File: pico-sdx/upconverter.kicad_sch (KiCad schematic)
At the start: 52 parts, among them T2 Transformer_SP_1S, U4 LM321, U5 74HC74, U6 4066, U7 OPA1602

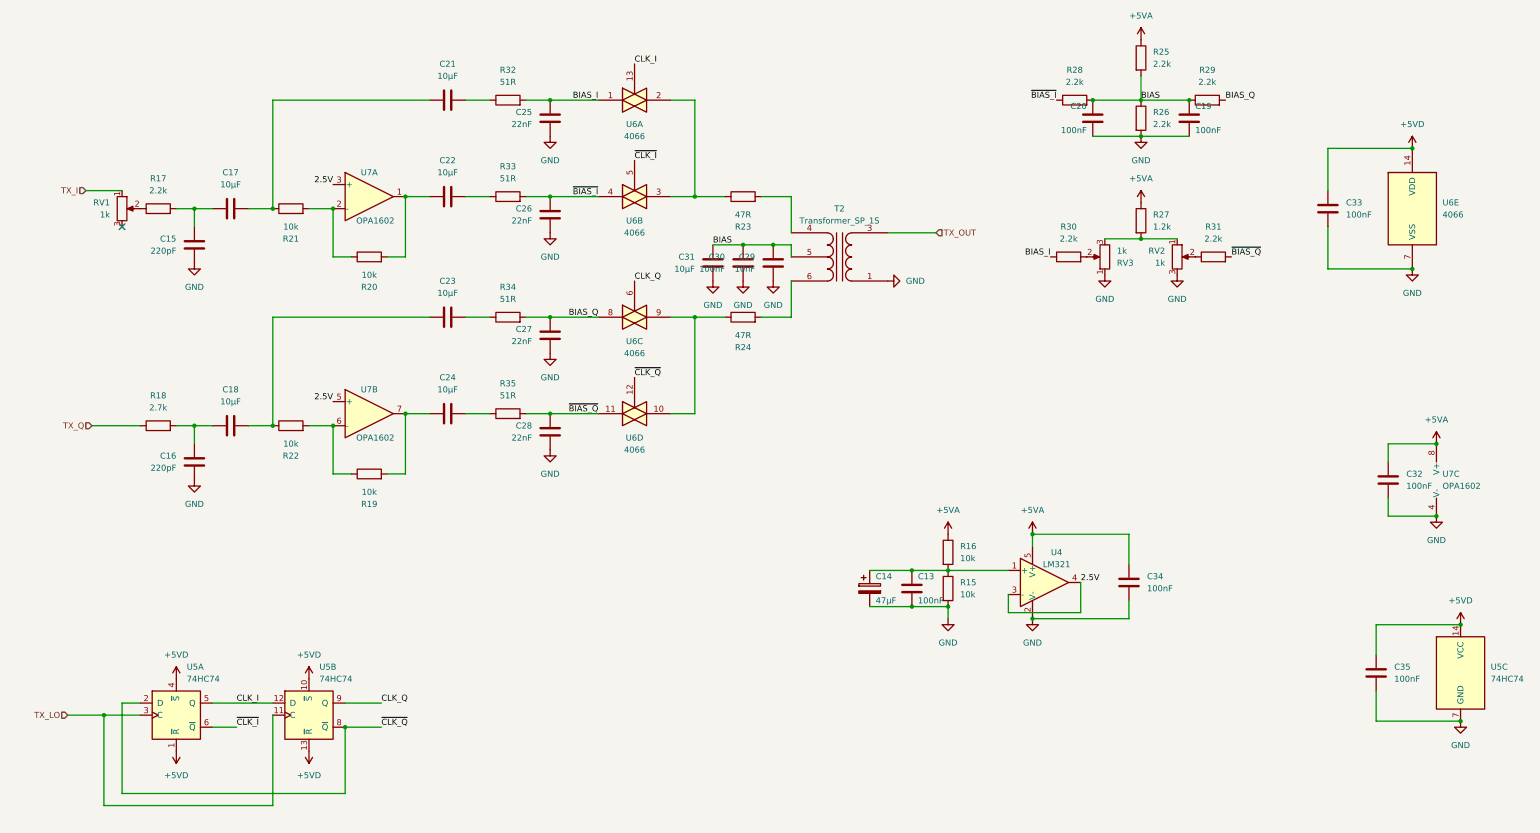
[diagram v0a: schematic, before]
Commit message: add documentation and RaspberryPi Pico
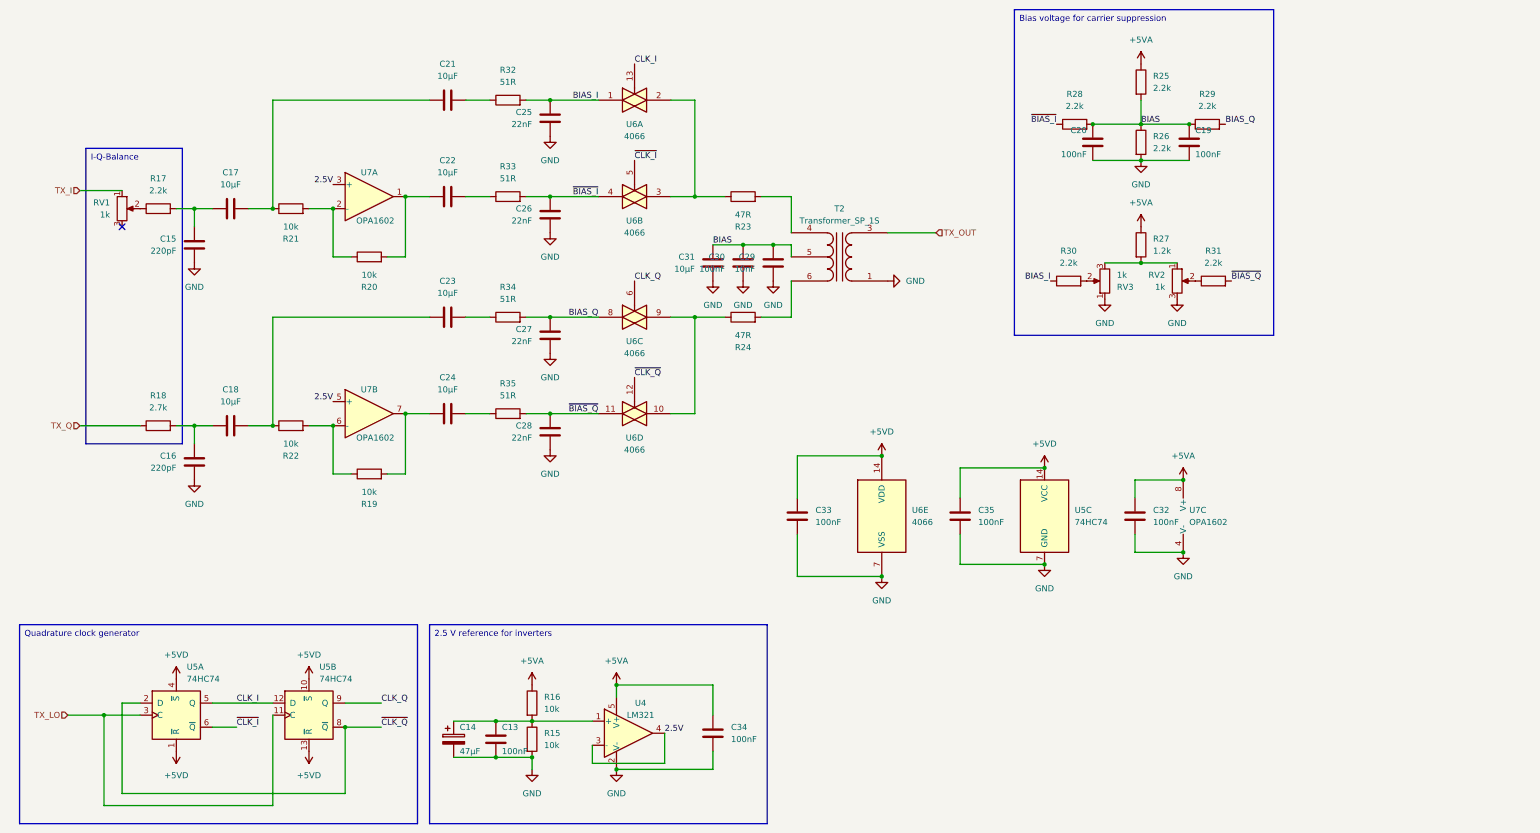
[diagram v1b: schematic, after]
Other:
- moved on the sheet: C13, C14, C19, C20, C32, C33, C34, C35, R15, R16, R25, R26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

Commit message: routed with filter relays without PA
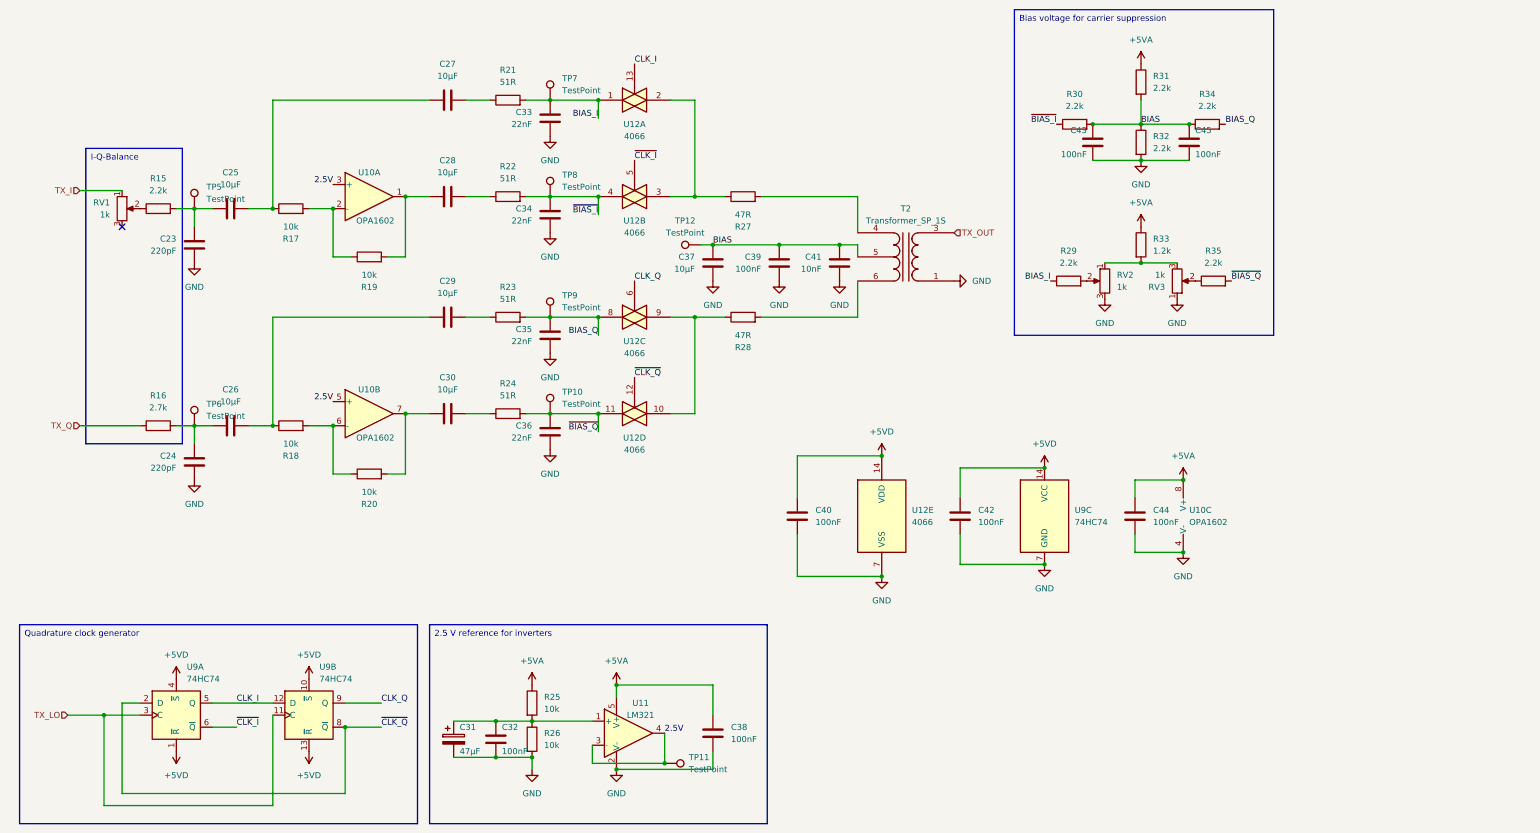
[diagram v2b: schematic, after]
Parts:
- added TP10, TP11, TP12, TP5, TP6, TP7, TP8, TP9: TestPoint, TestPoint:TestPoint_Loop_D1.80mm_Drill1.0mm_Beaded, symbol Connector:TestPoint
- renumbered C15 to C23, C16 to C24, C17 to C25, C18 to C26, C21 to C27, C22 to C28, C23 to C29, C24 to C30, C14 to C31, C13 to C32, C25 to C33, C26 to C34, C27 to C35, C28 to C36, C31 to C37, C34 to C38, C30 to C39, C33 to C40, C29 to C41, C35 to C42, C20 to C43, C32 to C44, C19 to C45, R17 to R15, R18 to R16, R21 to R17, R22 to R18, R20 to R19, R19 to R20, R32 to R21, R33 to R22, R34 to R23, R35 to R24, R16 to R25, R15 to R26, R23 to R27, R24 to R28, R30 to R29, R28 to R30, R25 to R31, R26 to R32, R27 to R33, R29 to R34, R31 to R35, RV3 to RV2, RV2 to RV3, U7 to U10, U4 to U11, U6 to U12, U5 to U9
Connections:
- net 2.5V: now also TP11.1
- net BIAS: now also TP12.1
- net BIAS_I: now also TP7.1
- net BIAS_Q: now also TP9.1
- net GND: now also RV2.3, RV3.1; no longer RV2.1, RV3.3
- net ~{BIAS_I}: now also TP8.1
- net ~{BIAS_Q}: now also TP10.1
- net at C23.1, C25.1, R15.2: now also TP5.1
- net at C24.1, C26.1, R16.2: now also TP6.1
- new net: R33.2, RV2.1, RV3.3
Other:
- moved on the sheet: C39, C41, RV2, T2

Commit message: add active lowpass filter in upconverter branch
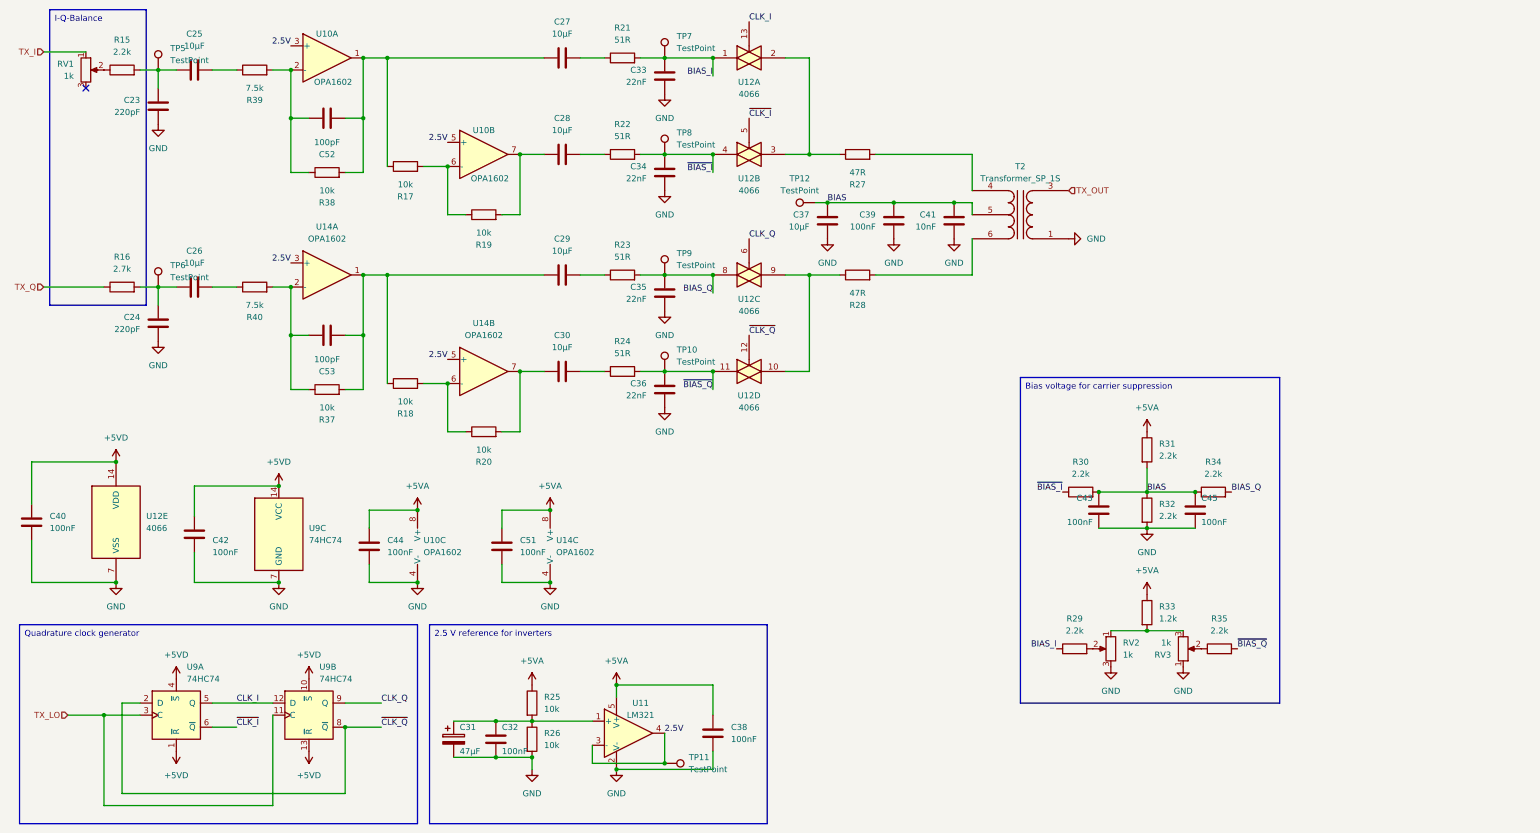
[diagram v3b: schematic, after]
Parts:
- added C51: 100nF, Capacitor_SMD:C_0603_1608Metric, symbol Device:C
- added C52, C53: 100pF, Capacitor_SMD:C_1206_3216Metric, symbol Device:C
- added R37, R38: 10k, Resistor_SMD:R_0603_1608Metric, symbol Device:R
- added R39, R40: 7.5k, Resistor_SMD:R_0603_1608Metric, symbol Device:R
- added U14: OPA1602, Package_SO:SOIC-8_3.9x4.9mm_P1.27mm, symbol Amplifier_Operational:OPA1602
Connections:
- net +5VA: now also C51.1, U14.8 (V+)
- net 2.5V: now also U14.3 (+), U14.5 (+)
- net GND: now also C51.2, U14.4 (V-)
- net at C28.1, R19.2: now also U10.7; no longer U10.1
- net at R18.2, R20.1: now also U14.6 (-); no longer U10.6 (-)
- net at C30.1, R20.2: now also U14.7; no longer U10.7
- net at C27.1, R17.1: now also U10.1, C52.2, R38.2; no longer C25.2
- net at R17.2, R19.1: now also U10.6 (-); no longer U10.2 (-)
- net at C29.1, R18.1: now also C53.2, R37.2, U14.1; no longer C26.2
- new net: C26.2, R40.1
- new net: C53.1, R37.1, R40.2, U14.2 (-)
- new net: C52.1, R38.1, R39.2, U10.2 (-)
- new net: C25.2, R39.1
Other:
- moved on the sheet: C23, C24, C25, C26, C27, C28, C29, C30, C33, C34, C35, C36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

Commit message: modular design
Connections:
- net +5VD renamed +3.3V
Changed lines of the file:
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@@
 	)
 	(symbol
-		(lib_id "power:+5VD")
+		(lib_id "power:+3.3V")
 		(at 76.2 172.72 180)
 		(unit 1)
@@
 			)
 		)
-		(property "Value" "+5VD"
+		(property "Value" "+3.3V"
 			(at 76.2 177.8 0)
 			(effects
@@
 			)
 		)
-		(property "Description" "Power symbol creates a global label with name \"+5VD\""
+		(property "Description" "Power symbol creates a global label with name \"+3.3V\""
 			(at 76.2 172.72 0)
 			(effects
@@
 	)
 	(symbol
-		(lib_id "power:+5VD")
+		(lib_id "power:+3.3V")
 		(at 69.85 116.84 0)
 		(unit 1)
@@
 			)
 		)
-		(property "Value" "+5VD"
+		(property "Value" "+3.3V"
 			(at 69.85 111.76 0)
 			(effects
@@
 			)
 		)
-		(property "Description" "Power symbol creates a global label with name \"+5VD\""
+		(property "Description" "Power symbol creates a global label with name \"+3.3V\""
 			(at 69.85 116.84 0)
 			(effects
@@
 	)
 	(symbol
-		(lib_id "power:+5VD")
+		(lib_id "power:+3.3V")
 		(at 76.2 157.48 0)
 		(unit 1)
@@
 			)
 		)
-		(property "Value" "+5VD"
+		(property "Value" "+3.3V"
 			(at 76.2 152.4 0)
 			(effects
@@
 			)
 		)
-		(property "Description" "Power symbol creates a global label with name \"+5VD\""
+		(property "Description" "Power symbol creates a global label with name \"+3.3V\""
 			(at 76.2 157.48 0)
 			(effects
@@
 	)
 	(symbol
-		(lib_id "power:+5VD")
+		(lib_id "power:+3.3V")
 		(at 48.26 172.72 180)
 		(unit 1)
@@
 			)
 		)
-		(property "Value" "+5VD"
+		(property "Value" "+3.3V"
 			(at 48.26 177.8 0)
 			(effects
@@
 			)
 		)
-		(property "Description" "Power symbol creates a global label with name \"+5VD\""
+		(property "Description" "Power symbol creates a global label with name \"+3.3V\""
 			(at 48.26 172.72 0)
 			(effects
@@
 	)
 	(symbol
-		(lib_id "power:+5VD")
+		(lib_id "power:+3.3V")
 		(at 35.56 111.76 0)
 		(unit 1)
@@
 			)
 		)
-		(property "Value" "+5VD"
+		(property "Value" "+3.3V"
 			(at 35.56 106.68 0)
 			(effects
@@
 			)
 		)
-		(property "Description" "Power symbol creates a global label with name \"+5VD\""
+		(property "Description" "Power symbol creates a global label with name \"+3.3V\""
 			(at 35.56 111.76 0)
 			(effects
@@
 	)
 	(symbol
-		(lib_id "power:+5VD")
+		(lib_id "power:+3.3V")
 		(at 48.26 157.48 0)
 		(unit 1)
@@
 			)
 		)
-		(property "Value" "+5VD"
+		(property "Value" "+3.3V"
 			(at 48.26 152.4 0)
 			(effects
@@
 			)
 		)
-		(property "Description" "Power symbol creates a global label with name \"+5VD\""
+		(property "Description" "Power symbol creates a global label with name \"+3.3V\""
 			(at 48.26 157.48 0)
 			(effects
